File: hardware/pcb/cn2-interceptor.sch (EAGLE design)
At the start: 4 parts, among them J1 JST-XH 4P, J2 JST-XH 4P, U1 XIAO ESP32-C3, U2 4CH BSS138

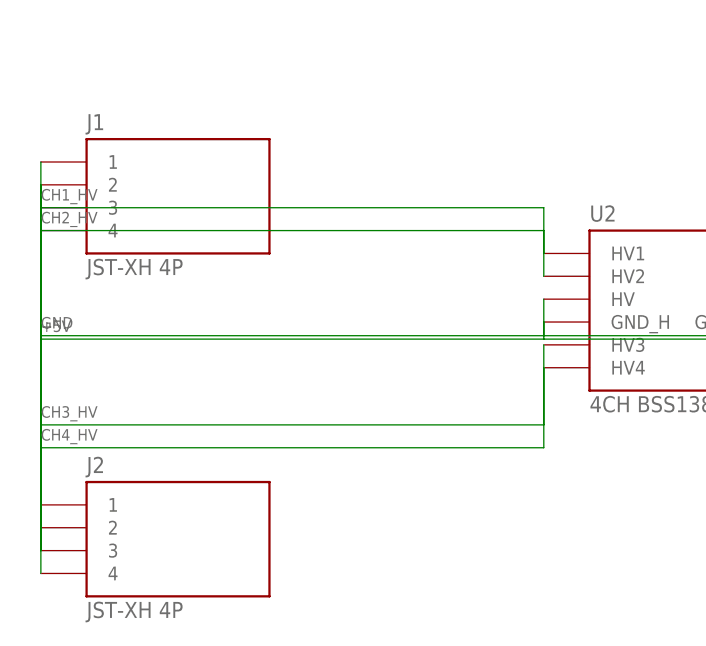
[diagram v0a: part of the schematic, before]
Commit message: pcb: 18.6 x 27 mm — connectors on opposite edges, flow relay dropped
39% less area and 41% narrower than the 31.5 x 26 board, which is the
dimension that decides whether it fits inside the appliance. Nothing about
the CN2 interception changes.

What made it small: the XIAO's two pad rows are 15.24 mm apart, so anything
standing beside them adds width directly, and the old board had a connector
on each side. Moving both to the top and bottom edges leaves nothing outside
the module except one routing lane -- shared by +5V on top and GND on the
bottom -- so the width is now pad block + lane + two edges, fully accounted
for and with nothing left in it. Each CN2 signal pin sits directly under the
middle corridor and climbs straight out of its own pad into its shifter pin,
turning once, so the four signals need no side lane at all.

The flow-meter relay (J3/J4) is gone, per Kai's call. Its six pins could not
share an edge with the CN2 connectors, so they were what forced the
connectors back onto the sides: that one feature cost more board than
everything else on it. The two hard-won warnings about it (the C3 is not 5 V
tolerant with no channel left to shift FV, and cutting the line strands the
meter's pull-up on the far side) are kept in the README for whoever re-adds
it.

Which connector goes on which edge is load-bearing, not cosmetic. Routing
forces LV1..LV4 onto D1..D4 in order -- they share a 0.94 mm channel and any
other order overlaps four deep -- and D1..D4 are GPIO3,4,5,6. The firmware's
as-built map puts the controller on GPIO5/6, which are the shifter's upper
channels, so the controller enters from the top. Get it backwards and the
board still works but only after swapping four defines, and a pin map that
disagrees with the copper does not announce itself: frames just stop
decoding. gen_pcb.py now reads firmware/include/config.h and fails on a
mismatch rather than leaving that to a comment.

Two new checks, both of which caught something real:

  MECHANICAL  th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
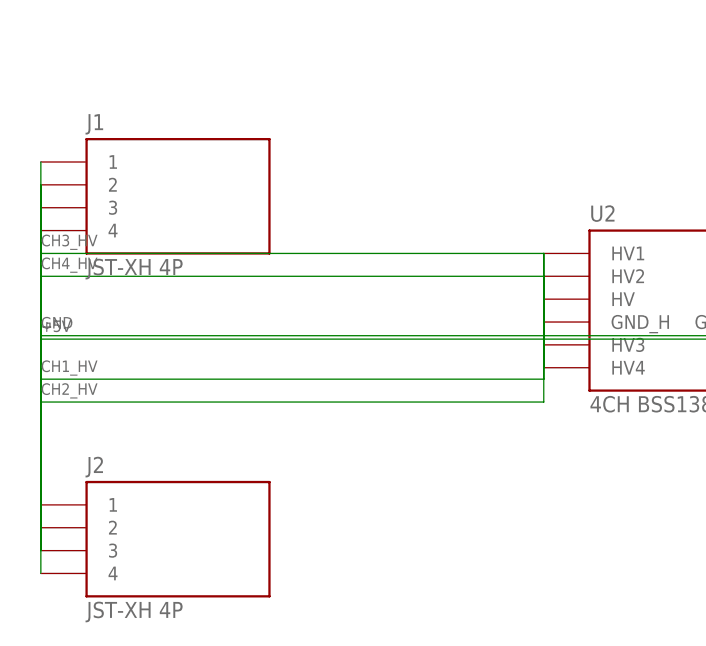
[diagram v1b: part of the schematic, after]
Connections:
- net CH1_HV: now also J2.1; no longer J1.1
- net CH2_HV: now also J2.2; no longer J1.2
- net CH3_HV: now also J1.1; no longer J2.1
- net CH4_HV: now also J1.2; no longer J2.2
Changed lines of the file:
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@@
 <net name="CH1_HV" class="0">
 <segment>
-<pinref part="J1" gate="G$1" pin="1"/>
+<pinref part="J2" gate="G$1" pin="1"/>
 <pinref part="U2" gate="G$1" pin="HV1"/>
-<wire x1="15.24" y1="119.38" x2="71.12" y2="119.38" width="0.1524" layer="91"/>
-<wire x1="15.24" y1="124.46" x2="15.24" y2="119.38" width="0.1524" layer="91"/>
-<wire x1="71.12" y1="114.30" x2="71.12" y2="119.38" width="0.1524" layer="91"/>
-<label x="15.24" y="120.18" size="1.27" layer="91"/>
+<wire x1="15.24" y1="100.33" x2="71.12" y2="100.33" width="0.1524" layer="91"/>
+<wire x1="15.24" y1="86.36" x2="15.24" y2="100.33" width="0.1524" layer="91"/>
+<wire x1="71.12" y1="114.30" x2="71.12" y2="100.33" width="0.1524" layer="91"/>
+<label x="15.24" y="101.13" size="1.27" layer="91"/>
 </segment></net>
 <net name="CH1_LV" class="0">
@@
 <net name="CH2_HV" class="0">
 <segment>
-<pinref part="J1" gate="G$1" pin="2"/>
+<pinref part="J2" gate="G$1" pin="2"/>
 <pinref part="U2" gate="G$1" pin="HV2"/>
-<wire x1="15.24" y1="116.84" x2="71.12" y2="116.84" width="0.1524" layer="91"/>
-<wire x1="15.24" y1="121.92" x2="15.24" y2="116.84" width="0.1524" layer="91"/>
-<wire x1="71.12" y1="111.76" x2="71.12" y2="116.84" width="0.1524" layer="91"/>
-<label x="15.24" y="117.64" size="1.27" layer="91"/>
+<wire x1="15.24" y1="97.79" x2="71.12" y2="97.79" width="0.1524" layer="91"/>
+<wire x1="15.24" y1="83.82" x2="15.24" y2="97.79" width="0.1524" layer="91"/>
+<wire x1="71.12" y1="111.76" x2="71.12" y2="97.79" width="0.1524" layer="91"/>
+<label x="15.24" y="98.59" size="1.27" layer="91"/>
 </segment></net>
 <net name="CH2_LV" class="0">
@@
 <net name="CH3_HV" class="0">
 <segment>
-<pinref part="J2" gate="G$1" pin="1"/>
+<pinref part="J1" gate="G$1" pin="1"/>
 <pinref part="U2" gate="G$1" pin="HV3"/>
-<wire x1="15.24" y1="95.25" x2="71.12" y2="95.25" width="0.1524" layer="91"/>
-<wire x1="15.24" y1="86.36" x2="15.24" y2="95.25" width="0.1524" layer="91"/>
-<wire x1="71.12" y1="104.14" x2="71.12" y2="95.25" width="0.1524" layer="91"/>
-<label x="15.24" y="96.05" size="1.27" layer="91"/>
+<wire x1="15.24" y1="114.30" x2="71.12" y2="114.30" width="0.1524" layer="91"/>
+<wire x1="15.24" y1="124.46" x2="15.24" y2="114.30" width="0.1524" layer="91"/>
+<wire x1="71.12" y1="104.14" x2="71.12" y2="114.30" width="0.1524" layer="91"/>
+<label x="15.24" y="115.10" size="1.27" layer="91"/>
 </segment></net>
 <net name="CH3_LV" class="0">
@@
 <net name="CH4_HV" class="0">
 <segment>
-<pinref part="J2" gate="G$1" pin="2"/>
+<pinref part="J1" gate="G$1" pin="2"/>
 <pinref part="U2" gate="G$1" pin="HV4"/>
-<wire x1="15.24" y1="92.71" x2="71.12" y2="92.71" width="0.1524" layer="91"/>
-<wire x1="15.24" y1="83.82" x2="15.24" y2="92.71" width="0.1524" layer="91"/>
-<wire x1="71.12" y1="101.60" x2="71.12" y2="92.71" width="0.1524" layer="91"/>
-<label x="15.24" y="93.51" size="1.27" layer="91"/>
+<wire x1="15.24" y1="111.76" x2="71.12" y2="111.76" width="0.1524" layer="91"/>
+<wire x1="15.24" y1="121.92" x2="15.24" y2="111.76" width="0.1524" layer="91"/>
+<wire x1="71.12" y1="101.60" x2="71.12" y2="111.76" width="0.1524" layer="91"/>
+<label x="15.24" y="112.56" size="1.27" layer="91"/>
 </segment></net>
 <net name="CH4_LV" class="0">
